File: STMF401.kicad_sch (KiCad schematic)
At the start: 26 parts, among them J6 Conn_01x04_Pin, U7 STM32F407VETx, Y1 X322525MQB4SI, Y2 SMD03215C2

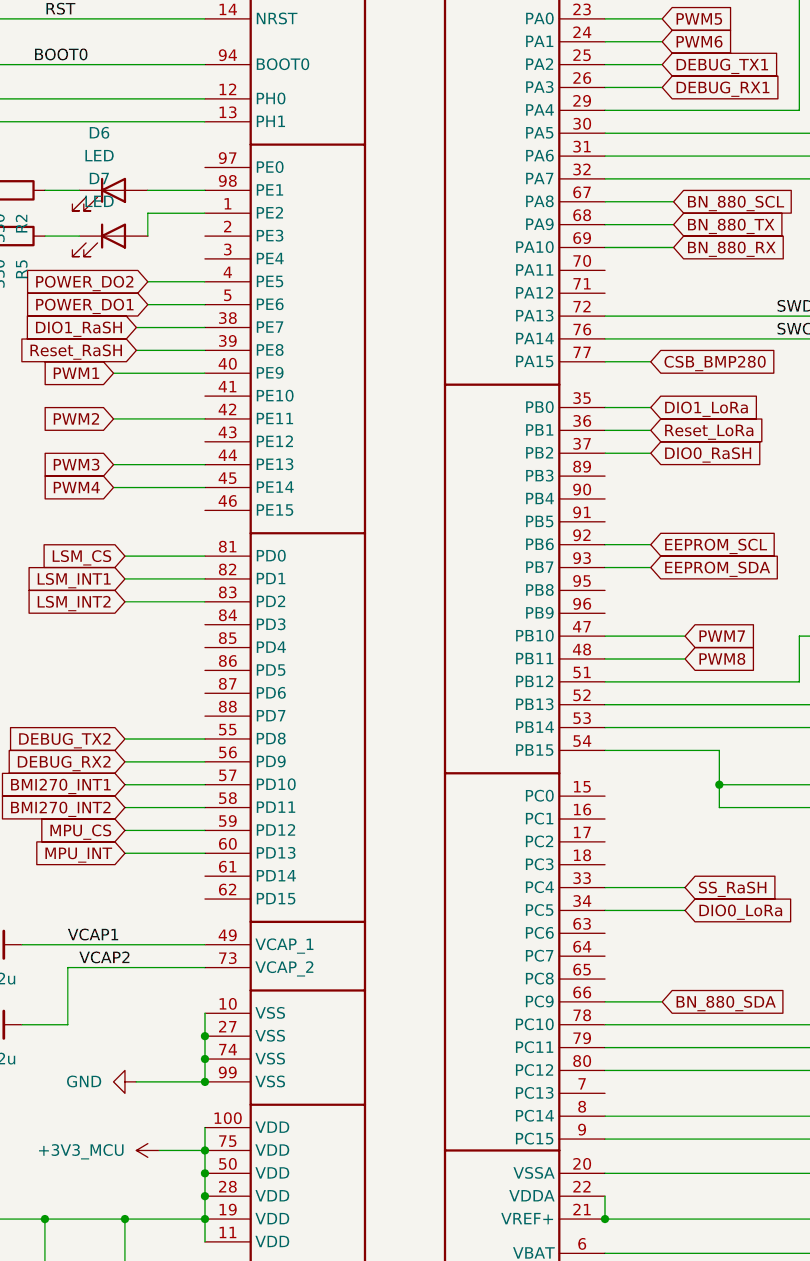
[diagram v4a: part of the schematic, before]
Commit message: feat: Разведены линии питания
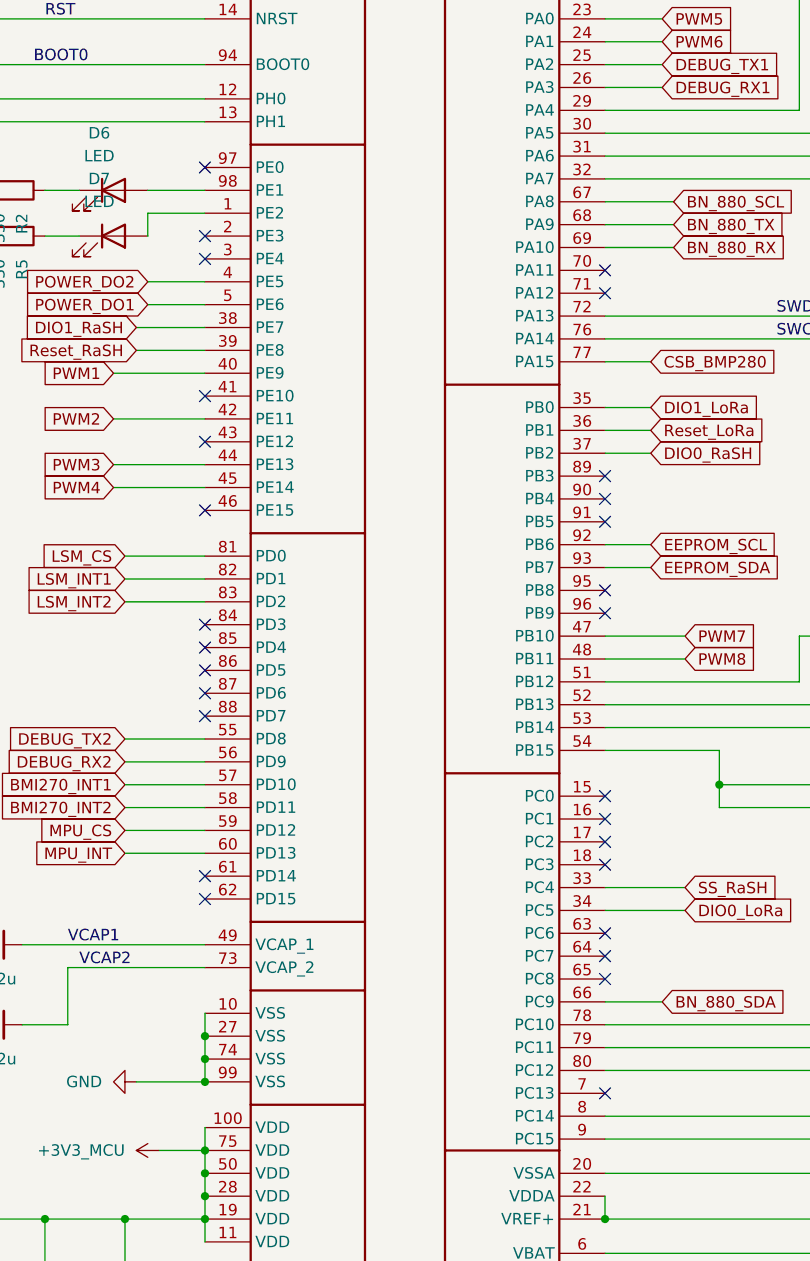
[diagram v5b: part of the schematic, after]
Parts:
- VD14: footprint Package_TO_SOT_SMD:SOT-23_Handsoldering -> Package_TO_SOT_SMD:SOT-23
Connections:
- no-connect marks 0 -> 28
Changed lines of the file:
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@@
 		(color 0 0 0 0)
 	)
+	(no_connect
+		(at 99.06 105.41)
+	)
+	(no_connect
+		(at 99.06 95.25)
+	)
+	(no_connect
+		(at 143.51 78.74)
+	)
+	(no_connect
+		(at 143.51 93.98)
+	)
+	(no_connect
+		(at 143.51 147.32)
+	)
+	(no_connect
+		(at 99.06 69.85)
+	)
+	(no_connect
+		(at 143.51 129.54)
+	)
+	(no_connect
+		(at 99.06 74.93)
+	)
+	(no_connect
+		(at 99.06 44.45)
+	)
+	(no_connect
+		(at 143.51 132.08)
+	)
+	(no_connect
+		(at 143.51 91.44)
+	)
+	(no_connect
+		(at 99.06 123.19)
+	)
+	(no_connect
+		(at 143.51 134.62)
+	)
+	(no_connect
+		(at 143.51 116.84)
+	)
+	(no_connect
+		(at 99.06 125.73)
+	)
+	(no_connect
+		(at 99.06 52.07)
+	)
+	(no_connect
+		(at 143.51 121.92)
+	)
+	(no_connect
+		(at 99.06 100.33)
+	)
+	(no_connect
+		(at 99.06 102.87)
+	)
+	(no_connect
+		(at 143.51 119.38)
+	)
+	(no_connect
+		(at 143.51 114.3)
+	)
+	(no_connect
+		(at 99.06 82.55)
+	)
+	(no_connect
+		(at 99.06 97.79)
+	)
+	(no_connect
+		(at 143.51 81.28)
+	)
+	(no_connect
+		(at 143.51 55.88)
+	)
+	(no_connect
+		(at 143.51 58.42)
+	)
+	(no_connect
+		(at 99.06 54.61)
+	)
+	(no_connect
+		(at 143.51 83.82)
+	)
 	(wire
 		(pts
@@
 			)
 		)
-		(property "Footprint" "Package_TO_SOT_SMD:SOT-23_Handsoldering"
+		(property "Footprint" "Package_TO_SOT_SMD:SOT-23"
 			(at 186.69 72.39 0)
 			(hide yes)

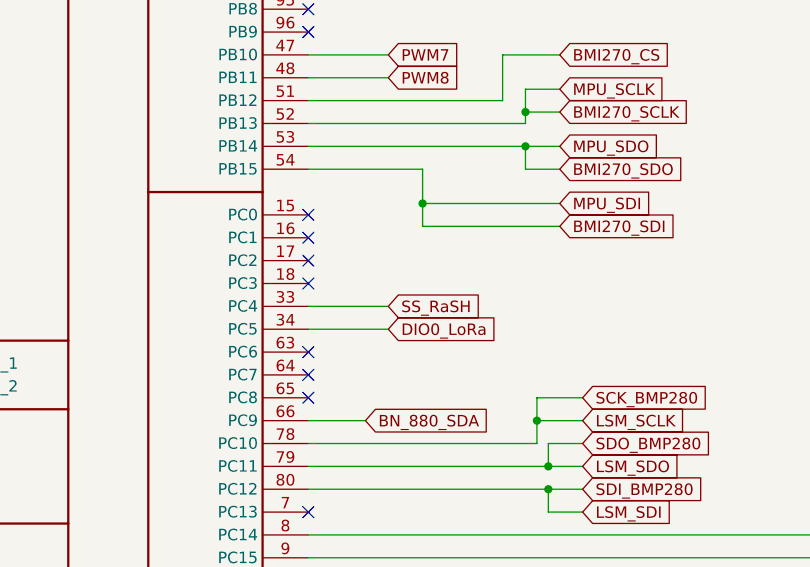
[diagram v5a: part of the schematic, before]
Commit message: feat: разведены линии для датчиков LSM и BMP280
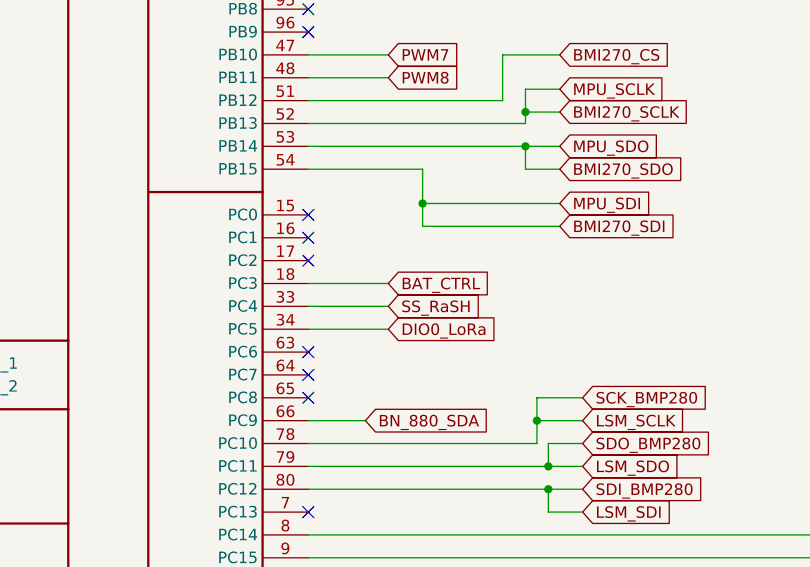
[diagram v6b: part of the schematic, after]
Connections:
- net BAT_CTRL: now reaches U7.18 (PC3)
- no-connect marks 28 -> 27
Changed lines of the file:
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@@
-	)
-	(no_connect
-		(at 143.51 121.92)
 	)
 	(no_connect
@@
 		(pts
 			(xy 167.64 100.33) (xy 167.64 102.87)
+		)
+		(stroke
+			(width 0)
+			(type default)
+		)
+	)
+	(wire
+		(pts
+			(xy 143.51 121.92) (xy 152.4 121.92)
 		)
 		(stroke
@@
 			(hide yes)
 			(show_name no)
+			(do_not_autoplace no)
+			(effects
+				(font
+					(size 1.27 1.27)
+				)
+				(justify left)
+			)
+		)
+	)
+	(global_label "BAT_CTRL"
+		(shape input)
+		(at 152.4 121.92 0)
+		(fields_autoplaced yes)
+		(effects
+			(font
+				(size 1.27 1.27)
+			)
+			(justify left)
+		)
+		(property "Intersheetrefs" "${INTERSHEET_REFS}"
+			(at 164.2147 121.92 0)
+			(hide yes)
+			(show_name no)
